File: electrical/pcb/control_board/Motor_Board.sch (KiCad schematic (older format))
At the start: 83 parts, among them J1 XT30-M, J10 Molex_172675-0613, J11 Molex_172675-0613, J12 TSW-104-07-F-T, J13 Molex_172675-0613, J14 Molex_172675-0613, J15 TSW-104-07-F-T, J16 277-11404-ND, J17 277-11404-ND, J18 277-11404-ND, J19 TSW-104-07-F-T, J2 XT30-F, J20 PEC08SAAN, J21 PPTC102LFBN-RC, J3 XT30-F, J4 XT30-F, J5 XT30-M, J6 ED2580-ND, J7 TSW-104-07-F-T, J8 Molex_172675-0613, J9 Molex_172675-0613, T1 test_point, T10 test_point, T11 test_point, T12 test_point, T2 test_point, T3 test_point, T4 test_point, T5 test_point, T6 test_point, T7 test_point, T8 test_point, T9 test_point, U1 INA260, U2 PCA9685, U3 D24V22Fx, U4 D24V150Fx, U5 DC7G3HWA, y1 rover_silkscreen

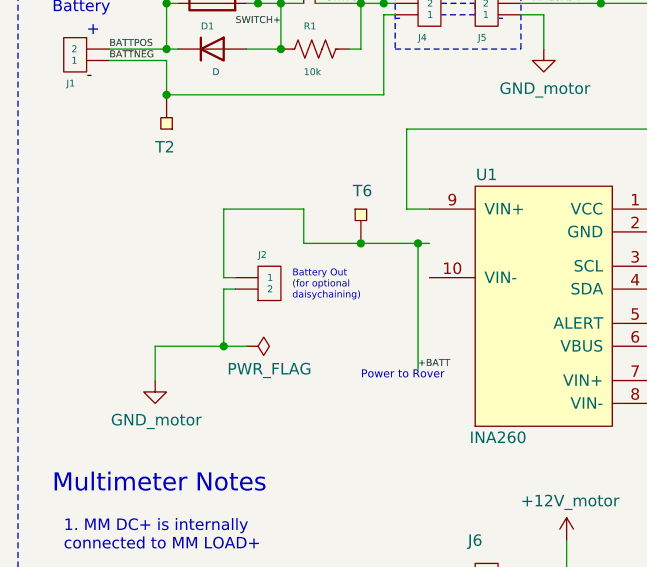
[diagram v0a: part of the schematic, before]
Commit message: Fix orientation of j2
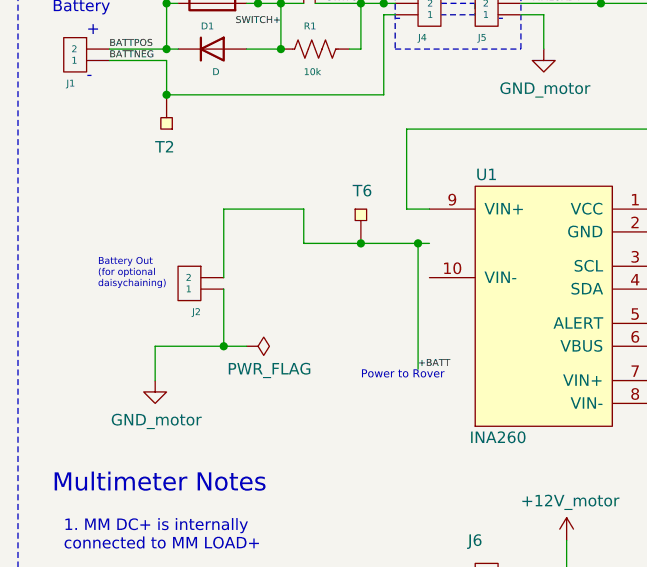
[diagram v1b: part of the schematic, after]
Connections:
- net +BATT: now also J2.2; no longer J2.1
- net GND_motor: now also J2.1; no longer J2.2
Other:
- moved on the sheet: J2
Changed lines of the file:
@@
 L JPL_Robotics_Lib:XT60-F J?
 U 1 1 60B75520
-P 2100 6950
+P 1750 6800
 AR Path="/60B75520" Ref="J?"  Part="1"
 AR Path="/60A51BAC/60B75520" Ref="J2"  Part="1"
-F 0 "J2" H 2150 7150 30  0000 R CNN
-F 1 "XT30-F" V 1950 7150 30  0001 R CNN
-F 2 "JPL Robotics:AMASS_XT30U-F_1x02_P5.0mm_Vertical" H 2100 7150 30  0001 C CNN
-F 3 "" H 2100 7150 30  0001 C CNN
-	1    2100 6950
-	-1   0    0    -1
+F 0 "J2" H 1800 7000 30  0000 R CNN
+F 1 "XT30-F" V 1600 7000 30  0001 R CNN
+F 2 "JPL Robotics:AMASS_XT30U-F_1x02_P5.0mm_Vertical" H 1750 7000 30  0001 C CNN
+F 3 "" H 1750 7000 30  0001 C CNN
+	1    1750 6800
+	1    0    0    1
 $EndComp
 Text Notes 2100 5350 0    50   ~ 0
 Switch
-Text Notes 2200 6950 0    30   ~ 0
+Text Notes 1350 6900 0    30   ~ 0
 Battery Out \n(for optional \ndaisychaining)
 Text Notes 3100 5750 0    50   ~ 0
@@
 Wire Wire Line
 	1600 7150 1900 7150
-Wire Wire Line
-	1900 6900 1950 6900
 $Comp
 L JPL_Robotics_Lib:GND_motor #PWR01
@@
 	1900 6550 1900 6850
 Wire Wire Line
-	1900 6850 1950 6850
-Wire Wire Line
 	2600 5700 2650 5700

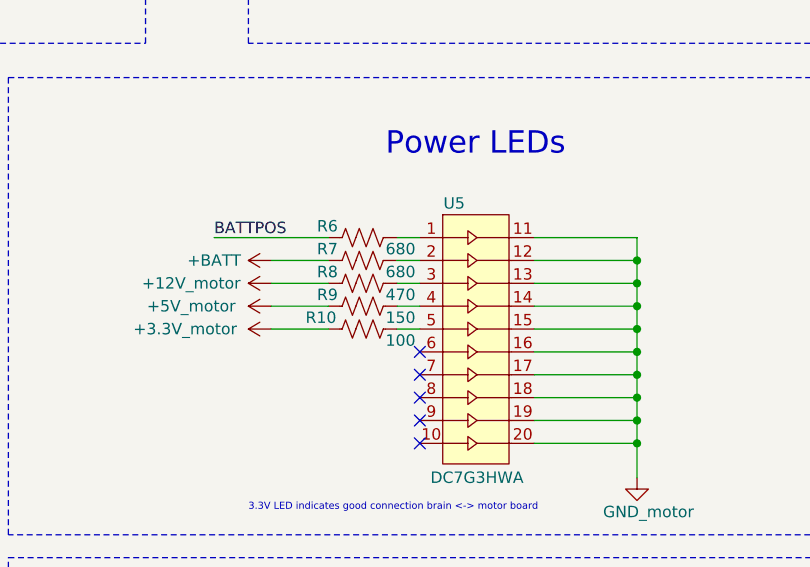
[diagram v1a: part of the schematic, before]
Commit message: Updating resistor values for u5
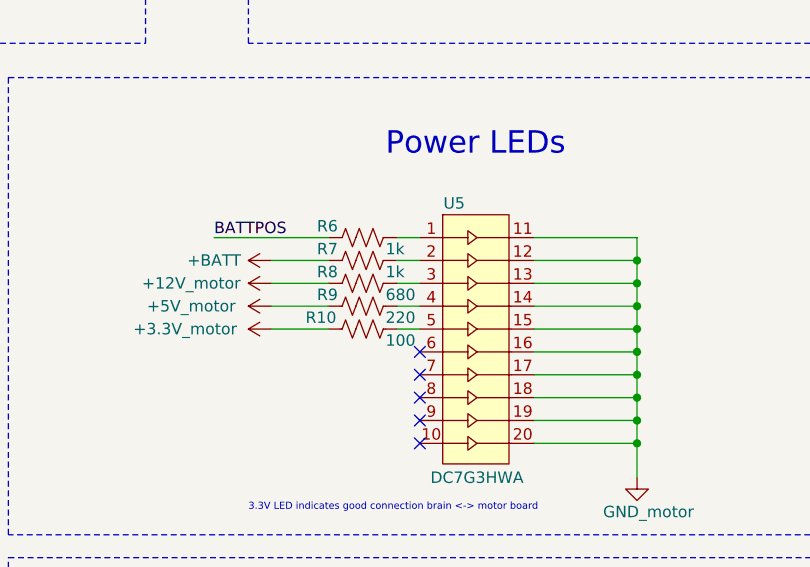
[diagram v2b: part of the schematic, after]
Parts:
- R6, R7: value 680 -> 1k
- R8: value 470 -> 680
- R9: value 150 -> 220
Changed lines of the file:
@@
 AR Path="/60A51BAC/6139BB6C" Ref="R6"  Part="1"
 F 0 "R6" V 13600 5400 50  0000 L CNN
-F 1 "680" V 13700 5700 50  0000 L CNN
+F 1 "1k" V 13700 5700 50  0000 L CNN
 F 2 "Resistor_THT:R_Axial_DIN0207_L6.3mm_D2.5mm_P7.62mm_Horizontal" V 13690 5590 50  0001 C CNN
 F 3 "~" H 13650 5600 50  0001 C CNN
@@
 AR Path="/60A51BAC/613EAEB5" Ref="R7"  Part="1"
 F 0 "R7" V 13600 5500 50  0000 L CNN
-F 1 "680" V 13700 5800 50  0000 L CNN
+F 1 "1k" V 13700 5800 50  0000 L CNN
 F 2 "Resistor_THT:R_Axial_DIN0207_L6.3mm_D2.5mm_P7.62mm_Horizontal" V 13690 5690 50  0001 C CNN
 F 3 "~" H 13650 5700 50  0001 C CNN
@@
 AR Path="/60A51BAC/615119DC" Ref="R8"  Part="1"
 F 0 "R8" V 13600 5600 50  0000 L CNN
-F 1 "470" V 13700 5900 50  0000 L CNN
+F 1 "680" V 13700 5900 50  0000 L CNN
 F 2 "Resistor_THT:R_Axial_DIN0207_L6.3mm_D2.5mm_P7.62mm_Horizontal" V 13690 5790 50  0001 C CNN
 F 3 "~" H 13650 5800 50  0001 C CNN
@@
 AR Path="/60A51BAC/61511E53" Ref="R9"  Part="1"
 F 0 "R9" V 13600 5700 50  0000 L CNN
-F 1 "150" V 13700 6000 50  0000 L CNN
+F 1 "220" V 13700 6000 50  0000 L CNN
 F 2 "Resistor_THT:R_Axial_DIN0207_L6.3mm_D2.5mm_P7.62mm_Horizontal" V 13690 5890 50  0001 C CNN
 F 3 "~" H 13650 5900 50  0001 C CNN

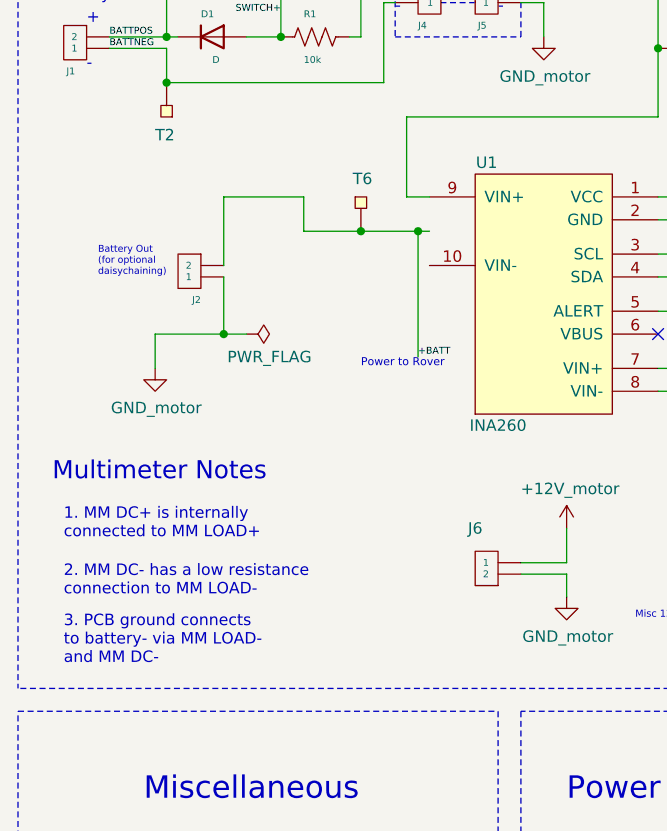
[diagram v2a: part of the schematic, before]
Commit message: Adding a bypass resistor for ina260
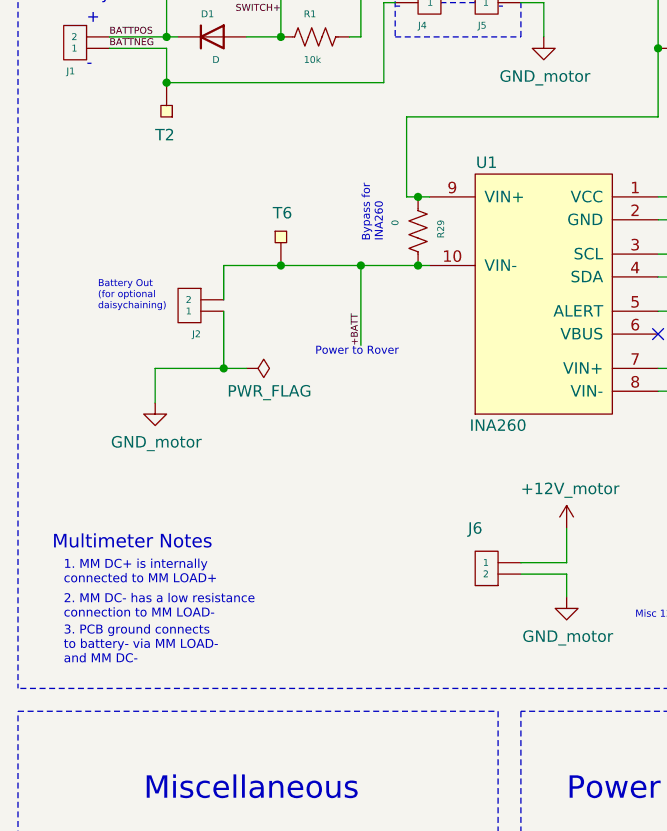
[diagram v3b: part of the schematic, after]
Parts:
- added R29: 0, Resistor_THT:R_Axial_DIN0207_L6.3mm_D2.5mm_P7.62mm_Horizontal, symbol Device:R_US
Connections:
- net +BATT: now also U1.10 (VIN-), R29.1
- net MMLOAD+: now also R29.2
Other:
- note added: "Bypass for \nINA260\n"
- moved on the sheet: J2, T6
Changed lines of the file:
@@
 Text Notes 1150 5700 0    50   ~ 0
 Battery
-Text Notes 1150 7800 0    79   ~ 0
+Text Notes 1150 8100 0    59   ~ 0
 Multimeter Notes
-Text Notes 1200 8050 0    50   ~ 0
+Text Notes 1200 8250 0    39   ~ 0
 1. MM DC+ is internally \nconnected to MM LOAD+
 Text Notes 1300 5800 0    50   ~ 0
@@
 Text Notes 1300 6000 0    50   ~ 0
 -
-Text Notes 1200 8600 0    50   ~ 0
-3. PCB ground connects\nto battery- via MM LOAD-\nand MM DC-
 Wire Wire Line
 	13850 3100 14150 3100
@@
 L JPL_Robotics_Lib:XT60-F J?
 U 1 1 60B75520
-P 1750 6800
+P 1750 6950
 AR Path="/60B75520" Ref="J?"  Part="1"
 AR Path="/60A51BAC/60B75520" Ref="J2"  Part="1"
-F 0 "J2" H 1800 7000 30  0000 R CNN
-F 1 "XT30-F" V 1600 7000 30  0001 R CNN
-F 2 "JPL Robotics:AMASS_XT30U-F_1x02_P5.0mm_Vertical" H 1750 7000 30  0001 C CNN
-F 3 "" H 1750 7000 30  0001 C CNN
-	1    1750 6800
+F 0 "J2" H 1800 7150 30  0000 R CNN
+F 1 "XT30-F" V 1600 7150 30  0001 R CNN
+F 2 "JPL Robotics:AMASS_XT30U-F_1x02_P5.0mm_Vertical" H 1750 7150 30  0001 C CNN
+F 3 "" H 1750 7150 30  0001 C CNN
+	1    1750 6950
 	1    0    0    1
 $EndComp
 Text Notes 2100 5350 0    50   ~ 0
 Switch
-Text Notes 1350 6900 0    30   ~ 0
+Text Notes 1350 7050 0    30   ~ 0
 Battery Out \n(for optional \ndaisychaining)
 Text Notes 3100 5750 0    50   ~ 0
@@
 Remeber this fuse goes with PN:\n507-2121-ND
 Wire Wire Line
-	1600 7300 1600 7150
-Wire Wire Line
-	1900 7150 1900 6900
-Wire Wire Line
-	1600 7150 1900 7150
+	1600 7450 1600 7300
+Wire Wire Line
+	1900 7300 1900 7050
+Wire Wire Line
+	1600 7300 1900 7300
 $Comp
 L JPL_Robotics_Lib:GND_motor #PWR01
 U 1 1 6124B41D
-P 1600 7300
-F 0 "#PWR01" H 1600 7050 50  0001 C CNN
-F 1 "GND_motor" H 1605 7127 50  0000 C CNN
-F 2 "" H 1600 7300 50  0001 C CNN
-F 3 "" H 1600 7300 50  0001 C CNN
-	1    1600 7300
+P 1600 7450
+F 0 "#PWR01" H 1600 7200 50  0001 C CNN
+F 1 "GND_motor" H 1605 7277 50  0000 C CNN
+F 2 "" H 1600 7450 50  0001 C CNN
+F 3 "" H 1600 7450 50  0001 C CNN
+	1    1600 7450
 	1    0    0    -1
 $EndComp
@@
 Text Label 4250 6650 2    30   ~ 0
 GND_motor
-Text Notes 1200 8300 0    50   ~ 0
+Text Notes 1200 8400 0    39   ~ 0
 2. MM DC- has a low resistance \nconnection to MM LOAD-
 Wire Wire Line
@@
 	3300 5850 3300 5700
 Wire Wire Line
-	1900 6550 1900 6850
-Wire Wire Line
 	2600 5700 2650 5700
 Wire Wire Line
@@
 	2500 5650 2300 5650
 Connection ~ 2500 5650
-Wire Wire Line
-	2750 6700 2800 6700
 Text Label 2150 5750 2    30   ~ 0
 SWITCH+
 Text Label 2350 5650 0    30   ~ 0
 SWITCH-
-Text Notes 2500 7300 0    35   ~ 0
+Text Notes 2300 7250 0    35   ~ 0
 Power to Rover
 Wire Wire Line
@@
 Text Notes 2800 10150 0    50   ~ 0
 \n
-Text Label 2750 7250 0    30   ~ 0
-+BATT
 Wire Wire Line
 	2700 6200 2700 6550
 Wire Wire Line
-	2700 6550 2800 6550
-Wire Wire Line
-	2750 6700 2500 6700
-Wire Wire Line
-	2250 6700 2250 6550
-Wire Wire Line
-	2250 6550 1900 6550
-Connection ~ 2750 6700
+	2700 6550 2750 6550
 $Comp
 L Device:R_US R?
@@
 todo: do we actually want to disconnect\n ground from pin 6?
 NoConn ~ 8100 7450
-Connection ~ 1900 7150
-Wire Wire Line
-	2000 7150 1900 7150
+Connection ~ 1900 7300
+Wire Wire Line
+	2000 7300 1900 7300
 $Comp
 L power:PWR_FLAG #FLG?
 U 1 1 60B75584
-P 2000 7150
+P 2000 7300
 AR Path="/60B75584" Ref="#FLG?"  Part="1"
 AR Path="/60A51BAC/60B75584" Ref="#FLG02"  Part="1"
-F 0 "#FLG02" H 2000 7225 50  0001 C CNN
-F 1 "PWR_FLAG" V 2100 7250 50  0000 C CNN
-F 2 "" H 2000 7150 50  0001 C CNN
-F 3 "~" H 2000 7150 50  0001 C CNN
-	1    2000 7150
+F 0 "#FLG02" H 2000 7375 50  0001 C CNN
+F 1 "PWR_FLAG" V 2100 7400 50  0000 C CNN
+F 2 "" H 2000 7300 50  0001 C CNN
+F 3 "~" H 2000 7300 50  0001 C CNN
+	1    2000 7300
 	0    1    1    0
 $EndComp
@@
 	4500 9700 4500 10050
 Wire Wire Line
-	2750 6700 2750 7250
-Wire Wire Line
 	14500 9150 14800 9150
 Wire Wire Line
@@
 L JPL_Robotics_Lib:test_point T6
 U 1 1 64361B1F
-P 2500 6550
-F 0 "T6" V 2550 6500 50  0000 L TNN
-F 1 "test_point" H 2650 6800 50  0001 C CNN
-F 2 "JPL Robotics:test_point" H 2450 6500 50  0001 C CNN
-F 3 "" H 2450 6500 50  0001 C CNN
-	1    2500 6550
+P 2150 6700
+F 0 "T6" V 2200 6650 50  0000 L TNN
+F 1 "test_point" H 2300 6950 50  0001 C CNN
+F 2 "JPL Robotics:test_point" H 2100 6650 50  0001 C CNN
+F 3 "" H 2100 6650 50  0001 C CNN
+	1    2150 6700
 	0    -1   -1   0
 $EndComp
-Connection ~ 2500 6700
-Wire Wire Line
-	2500 6700 2250 6700
 $Comp
 L JPL_Robotics_Lib:test_point T2
@@
 	0    -1   -1   0
 $EndComp
+Connection ~ 2150 6850
+Text Label 2500 7200 1    30   ~ 0
++BATT
+$Comp
+L Device:R_US R?
+U 1 1 63E66B4C
+P 2750 6700
+AR Path="/63E66B4C" Ref="R?"  Part="1"
+AR Path="/60A51BAC/63E66B4C" Ref="R29"  Part="1"
+F 0 "R29" V 2650 6650 30  0000 L CNN
+F 1 "0" V 2850 6650 30  0000 L CNN
+F 2 "Resistor_THT:R_Axial_DIN0207_L6.3mm_D2.5mm_P7.62mm_Horizontal" V 2790 6690 50  0001 C CNN
+F 3 "~" H 2750 6700 50  0001 C CNN
+	1    2750 6700
+	-1   0    0    1
+$EndComp
+Text Notes 1200 8600 0    39   ~ 0
+3. PCB ground connects\nto battery- via MM LOAD-\nand MM DC-
+Wire Wire Line
+	1900 6850 1900 7000
+Wire Wire Line
+	1900 6850 2150 6850
+Wire Wire Line
+	2150 6850 2500 6850
+Connection ~ 2750 6850
+Wire Wire Line
+	2750 6850 2800 6850
+Connection ~ 2750 6550
+Wire Wire Line
+	2750 6550 2800 6550
+Wire Wire Line
+	2500 6850 2500 7200
+Connection ~ 2500 6850
+Wire Wire Line
+	2500 6850 2750 6850
+Text Notes 2600 6750 1    35   ~ 0
+Bypass for \nINA260\n
 $EndSCHEMATC

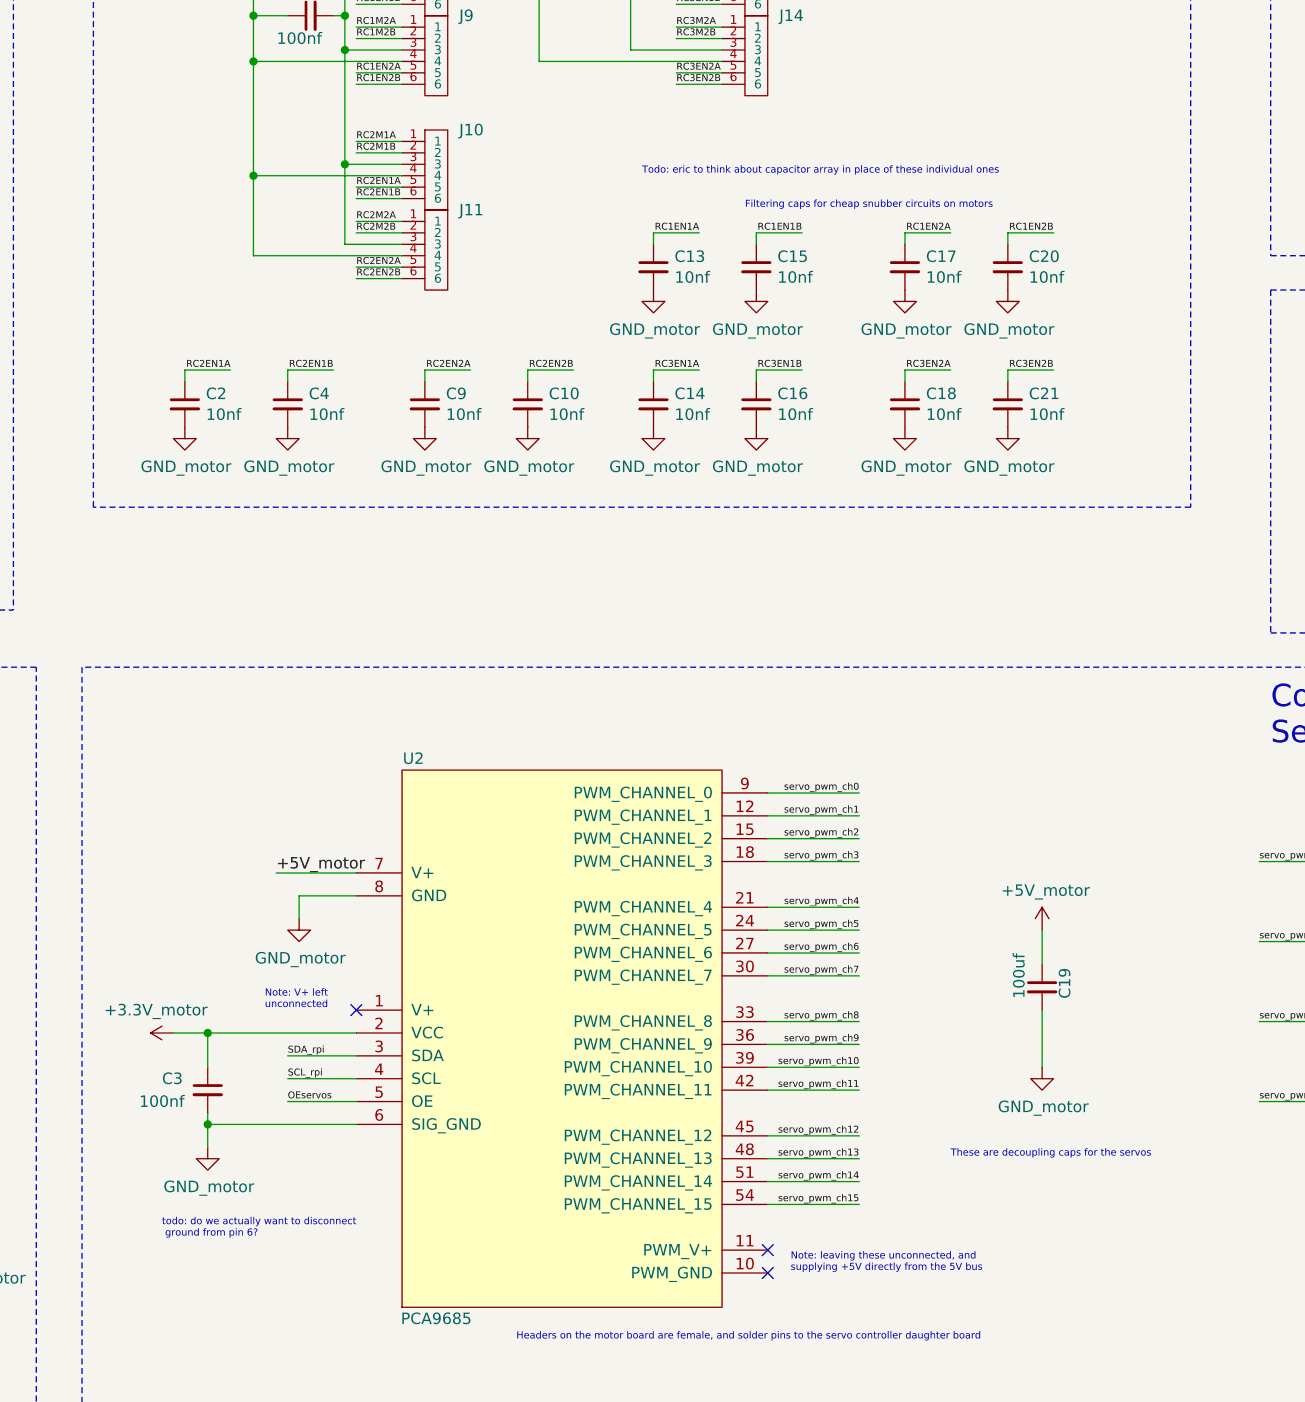
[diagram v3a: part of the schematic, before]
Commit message: deleting some todos
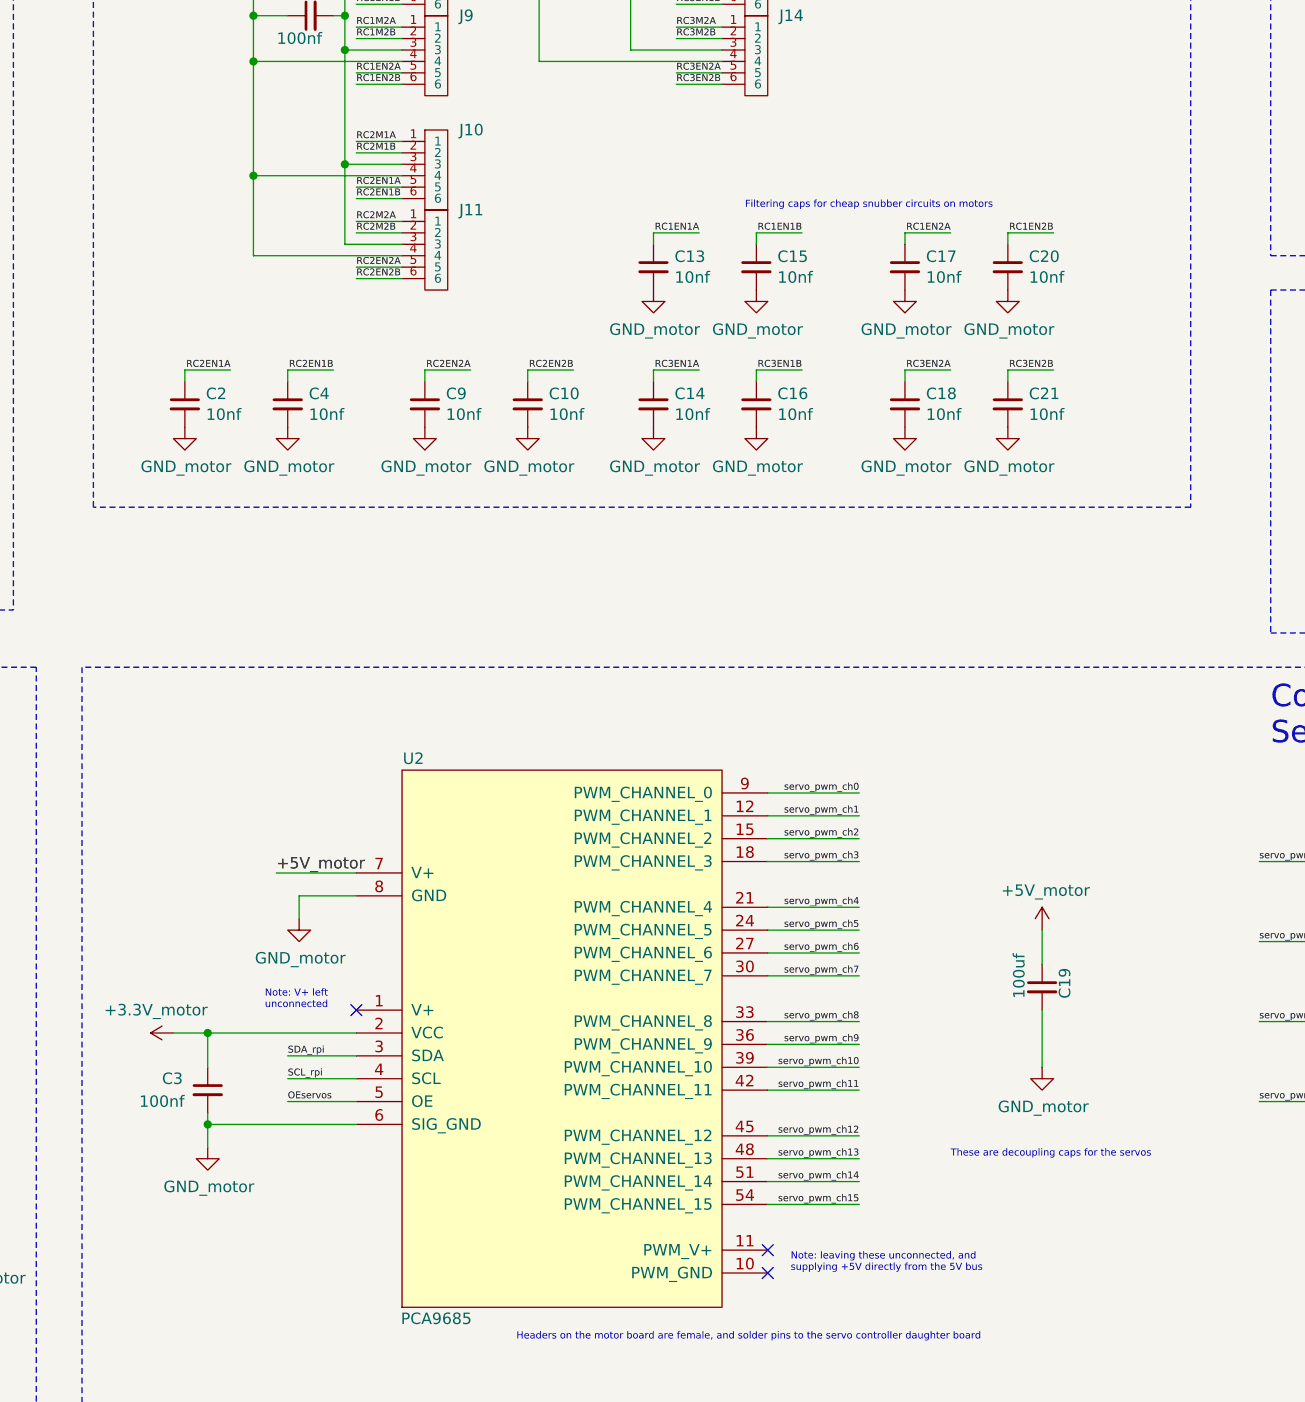
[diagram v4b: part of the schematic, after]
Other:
- note removed: "Todo: eric to think about capacitor array in place of these individual ones"
- note removed: "todo: do we actually want to disconnect\n ground from pin 6?"
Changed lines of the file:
@@
 Text Notes 6050 1500 0    31   ~ 0
 Todo: consolidate these caps into one master cap once we have a better idea of layout
-Text Notes 7550 2750 0    31   ~ 0
-Todo: eric to think about capacitor array in place of these individual ones
 $Comp
 L JPL_Robotics_Lib:D24V22Fx U3
@@
 Wire Wire Line
 	5650 6900 5650 7000
-Text Notes 5450 7400 0    31   ~ 0
-todo: do we actually want to disconnect\n ground from pin 6?
 NoConn ~ 8100 7450
 Connection ~ 1900 7300
